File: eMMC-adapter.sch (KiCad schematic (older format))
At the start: 29 parts, among them J1 SD_Card, U1 eMMC_5.1_BGA153

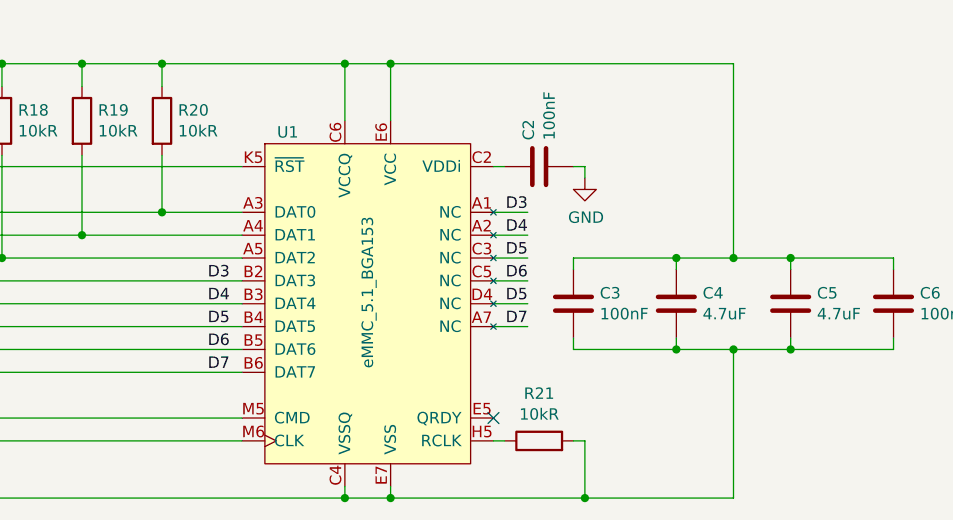
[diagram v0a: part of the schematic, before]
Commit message: Introduce separate VCC and VCCq domains
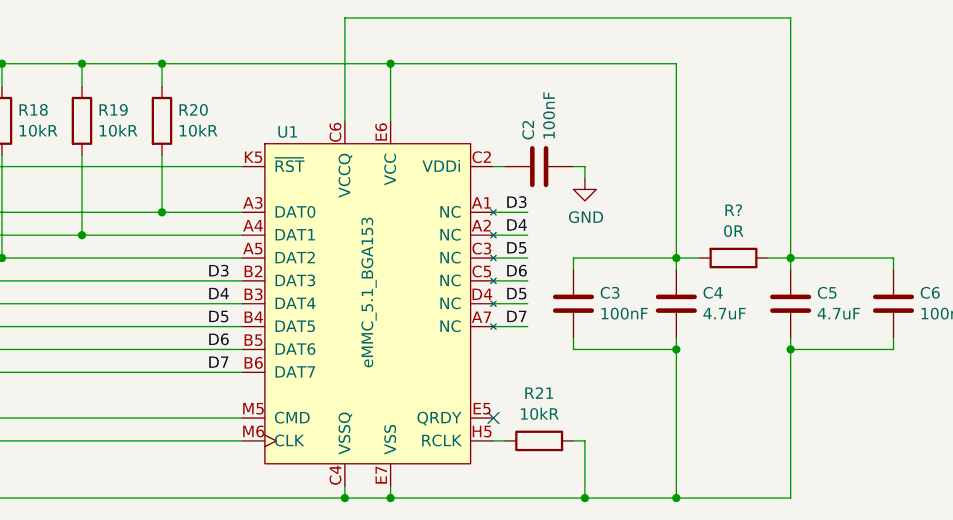
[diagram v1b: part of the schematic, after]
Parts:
- added R?: 0R, Resistor_SMD:R_0402_1005Metric, symbol Device:R
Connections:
- net VCC: now also R?.2; no longer C5.1, C6.1, U1.C6 (VCCQ), U1.M4 (VCCQ), U1.N4 (VCCQ), U1.P3 (VCCQ), U1.P5 (VCCQ)
- new net VCCQ: C5.1, C6.1, R?.1, U1.C6 (VCCQ), U1.M4 (VCCQ), U1.N4 (VCCQ), U1.P3 (VCCQ), U1.P5 (VCCQ)
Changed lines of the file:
@@
 Wire Wire Line
 	10750 3450 10300 3450
-Connection ~ 10050 3450
 Wire Wire Line
 	9800 3500 9800 3450
-Connection ~ 9800 3450
-Wire Wire Line
-	9800 3450 10050 3450
 Wire Wire Line
 	10300 3450 10300 3500
-Connection ~ 10300 3450
-Wire Wire Line
-	10300 3450 10050 3450
-Wire Wire Line
-	10050 3850 9800 3850
 Wire Wire Line
 	9350 3850 9350 3800
 Wire Wire Line
-	10050 3850 10300 3850
-Wire Wire Line
 	10750 3850 10750 3800
-Connection ~ 10050 3850
 Wire Wire Line
 	10300 3800 10300 3850
-Connection ~ 10300 3850
 Wire Wire Line
 	10300 3850 10750 3850
@@
 Wire Wire Line
 	8350 4500 8550 4500
-Wire Wire Line
-	8350 2600 8350 2850
-Wire Wire Line
-	8350 2600 8550 2600
-Connection ~ 8350 2600
-Wire Wire Line
-	10050 2600 10050 3450
-Wire Wire Line
-	10050 3850 10050 4500
 Connection ~ 8550 4500
 Wire Wire Line
 	8550 2600 8550 2850
-Connection ~ 8550 2600
-Wire Wire Line
-	8550 2600 10050 2600
 Text Label 2850 2600 0    50   ~ 0
 VDD
@@
 	7550 2700 7550 2600
 Wire Wire Line
-	7550 2600 8350 2600
-Wire Wire Line
 	7550 3000 7550 3250
 $Comp
@@
 Wire Wire Line
 	4750 3000 4750 4150
-Wire Wire Line
-	10050 4500 9400 4500
 Wire Wire Line
 	4750 2600 4400 2600
@@
 	2800 3550 2800 3850
 Connection ~ 2800 3850
+Wire Wire Line
+	9800 3850 9800 4500
+Wire Wire Line
+	9800 4500 9400 4500
+Wire Wire Line
+	10300 3850 10300 4500
+Wire Wire Line
+	10300 4500 9800 4500
+Connection ~ 10300 3850
+Connection ~ 9800 4500
+Wire Wire Line
+	8550 2600 9800 2600
+Wire Wire Line
+	9800 2600 9800 3450
+Connection ~ 8550 2600
+Connection ~ 9800 3450
+Wire Wire Line
+	7550 2600 8550 2600
+Wire Wire Line
+	8350 2850 8350 2400
+Wire Wire Line
+	8350 2400 10300 2400
+Wire Wire Line
+	10300 2400 10300 3450
+Connection ~ 10300 3450
+$Comp
+L Device:R R?
+U 1 1 5FD338E7
+P 10050 3450
+F 0 "R?" V 9843 3450 50  0000 C CNN
+F 1 "0R" V 9934 3450 50  0000 C CNN
+F 2 "Resistor_SMD:R_0402_1005Metric" V 9980 3450 50  0001 C CNN
+F 3 "~" H 10050 3450 50  0001 C CNN
+F 4 "C17168" V 10050 3450 50  0001 C CNN "LCSC"
+	1    10050 3450
+	0    1    1    0
+$EndComp
+Wire Wire Line
+	10200 3450 10300 3450
+Wire Wire Line
+	9900 3450 9800 3450
 $EndSCHEMATC

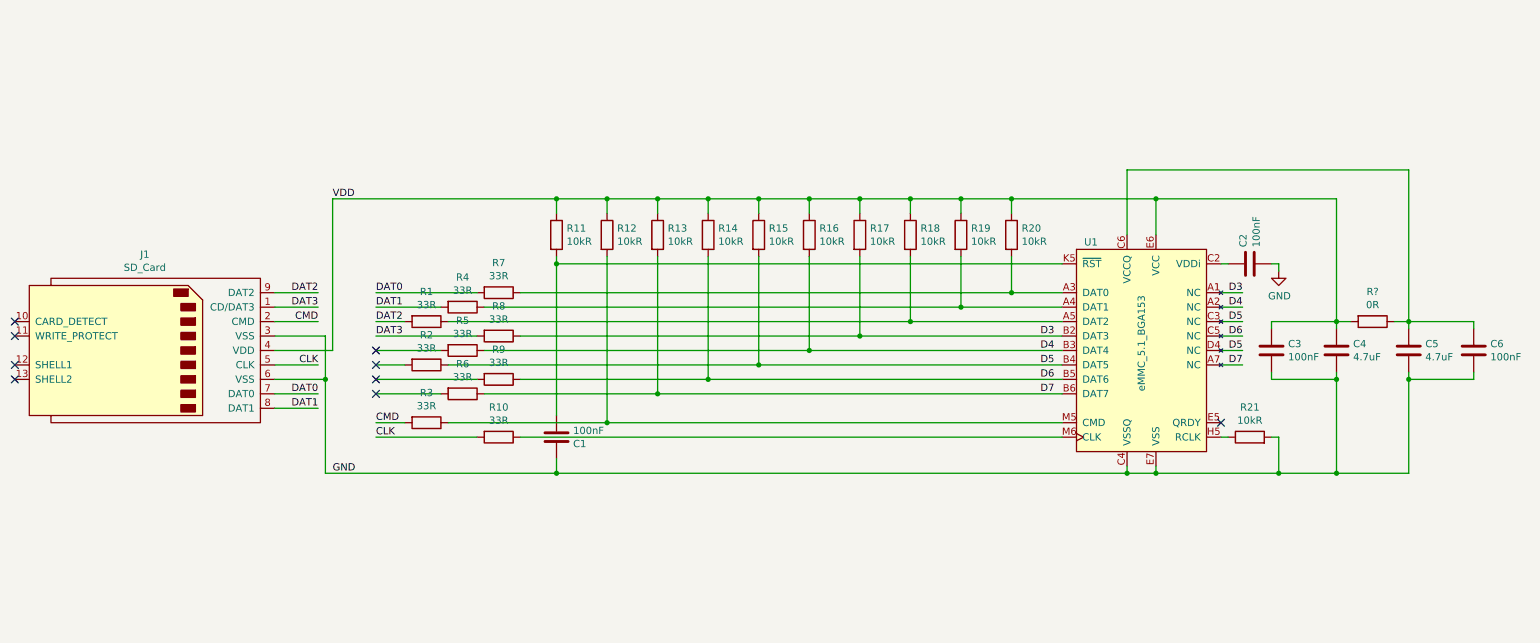
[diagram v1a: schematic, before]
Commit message: Panelize
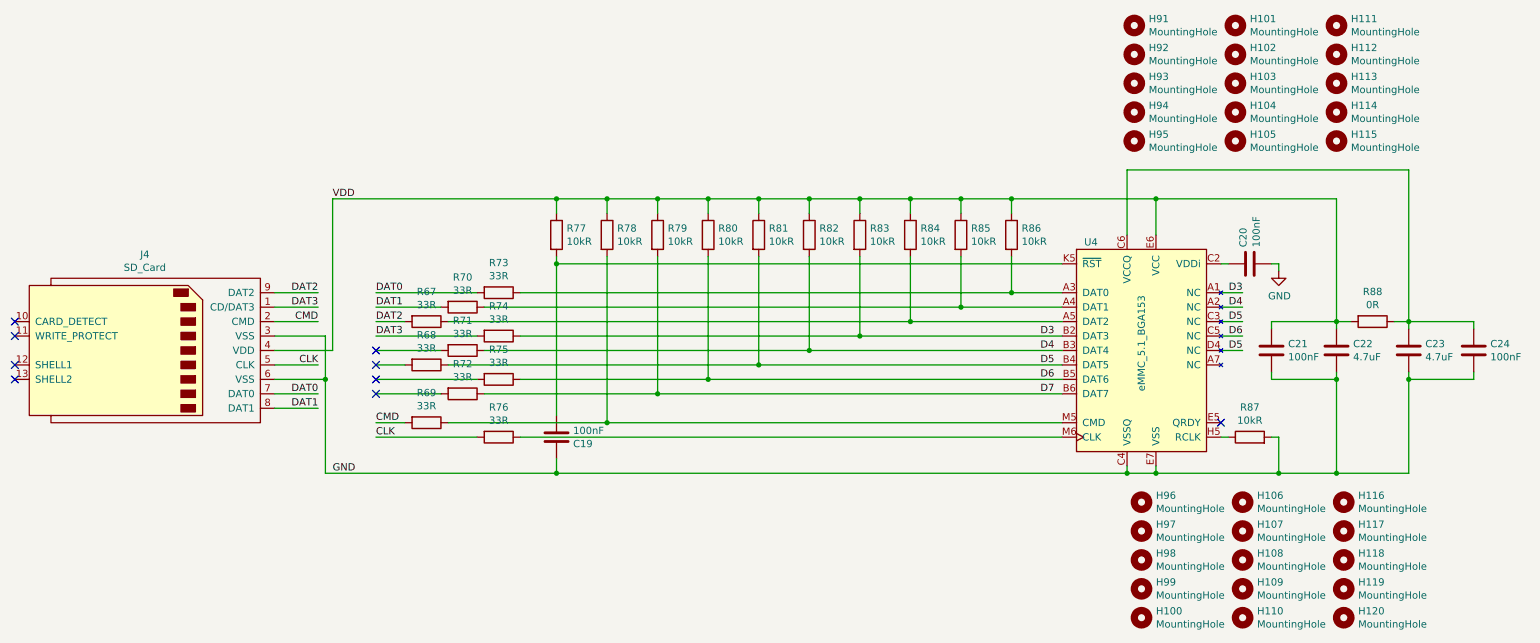
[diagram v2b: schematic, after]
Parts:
- added H1, H10, H11, H12, H13, H14, H15, H16, H17, H18, H19, H2, H20, H21, H22, H23, H24, H25, H26, H27, H28, H29, H3, H30, H4, H5, H6, H7, H8, H9: MountingHole, Perforation:Perforation_0.4mm, symbol Mechanical:MountingHole
- U1: LCSC (none) -> C391256
- gave numbers to parts that had none: 1
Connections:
- net D7: no longer U1.A7 (NC)

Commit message: Repurpose for ESP32 WiFi SDIO card
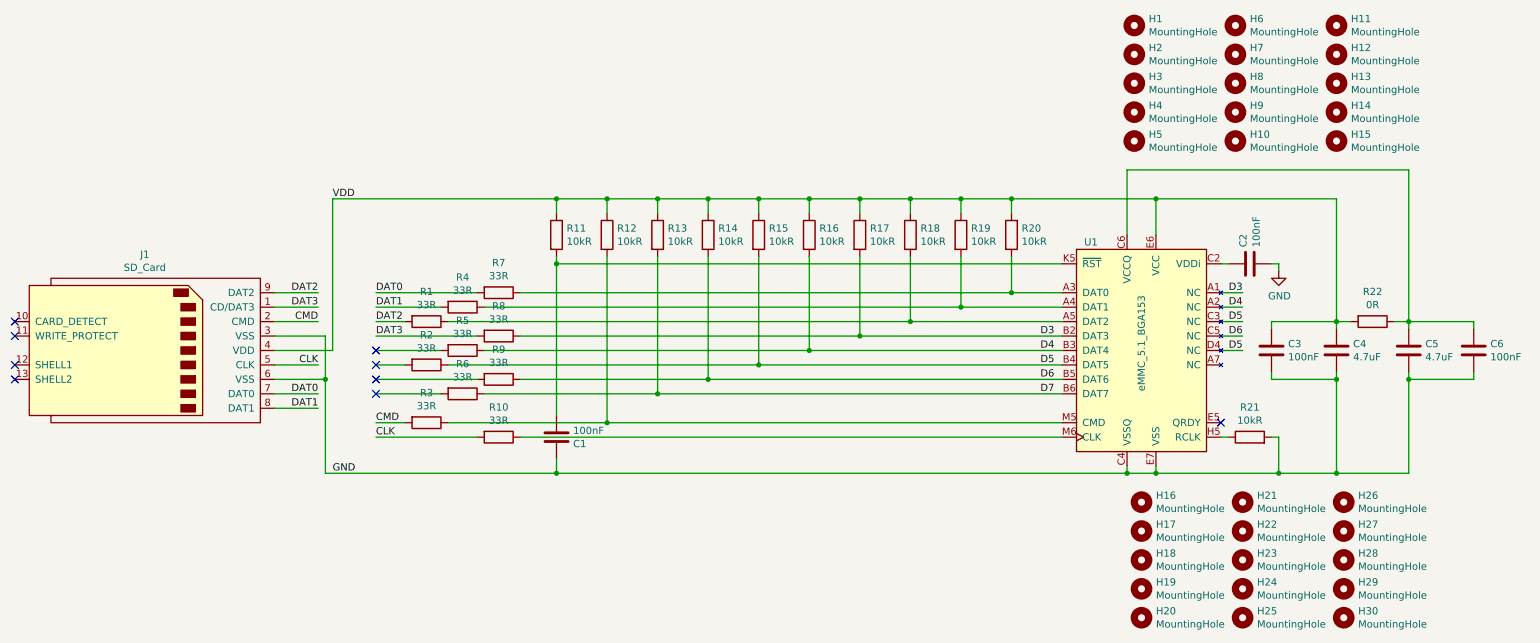
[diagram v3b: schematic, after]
